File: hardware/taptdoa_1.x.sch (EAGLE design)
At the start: 78 parts, among them J5 105017-0001, U1 SN74HCT245PWR, U2 AP2112K-3.3TRG1, U3 STM32F103RBT6, Y1 8MHz

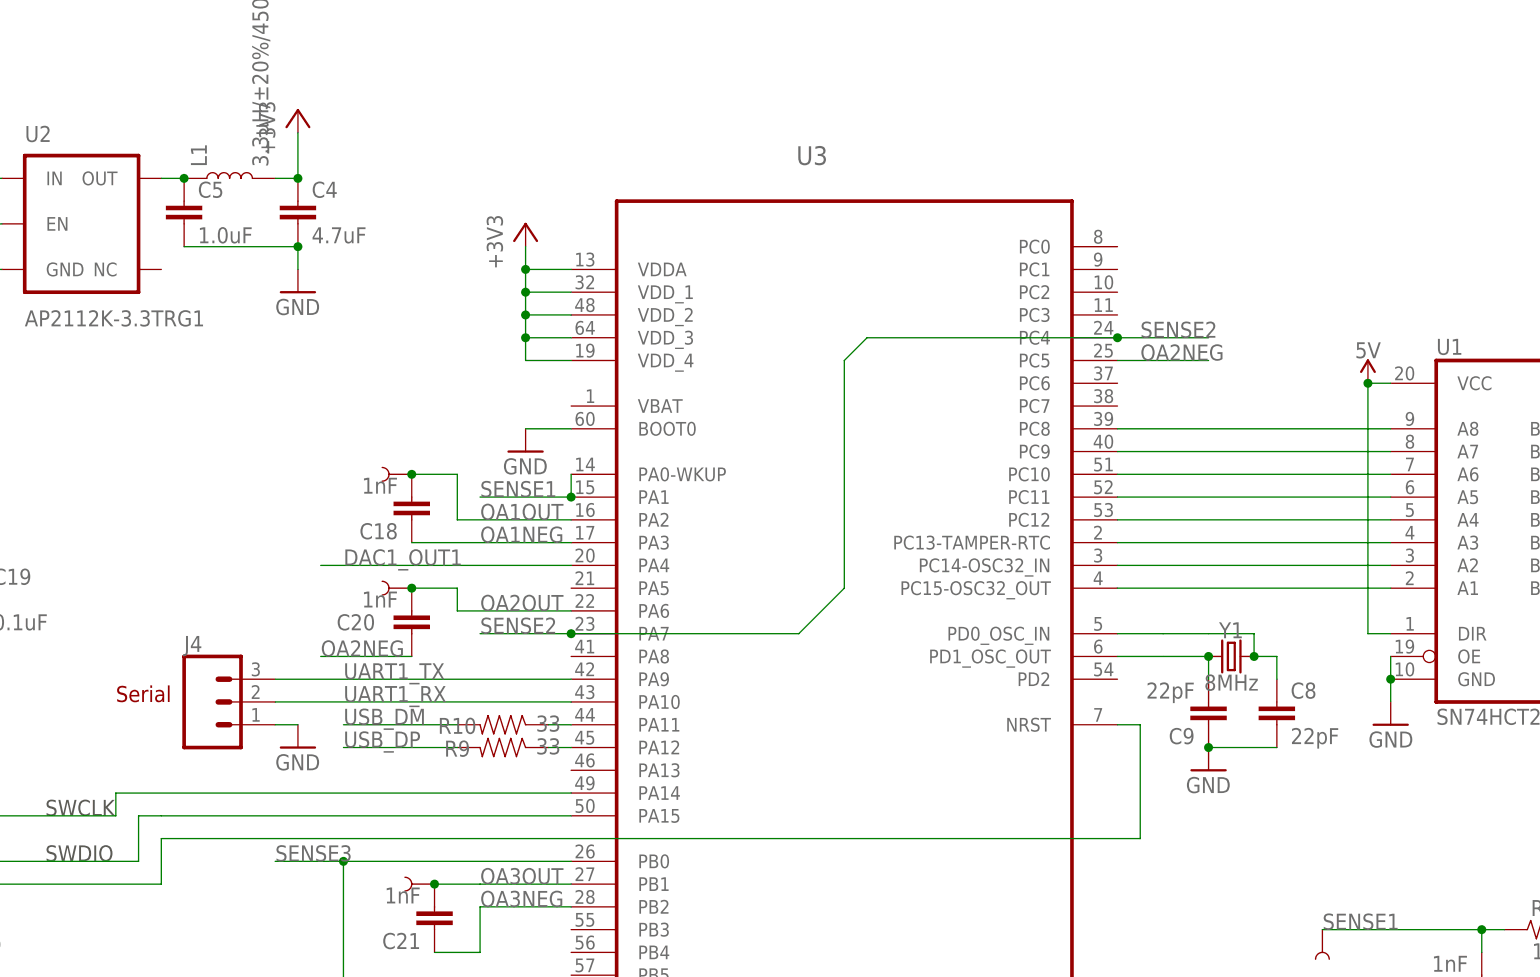
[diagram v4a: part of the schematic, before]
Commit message: new board rev with leds, fix swd pins
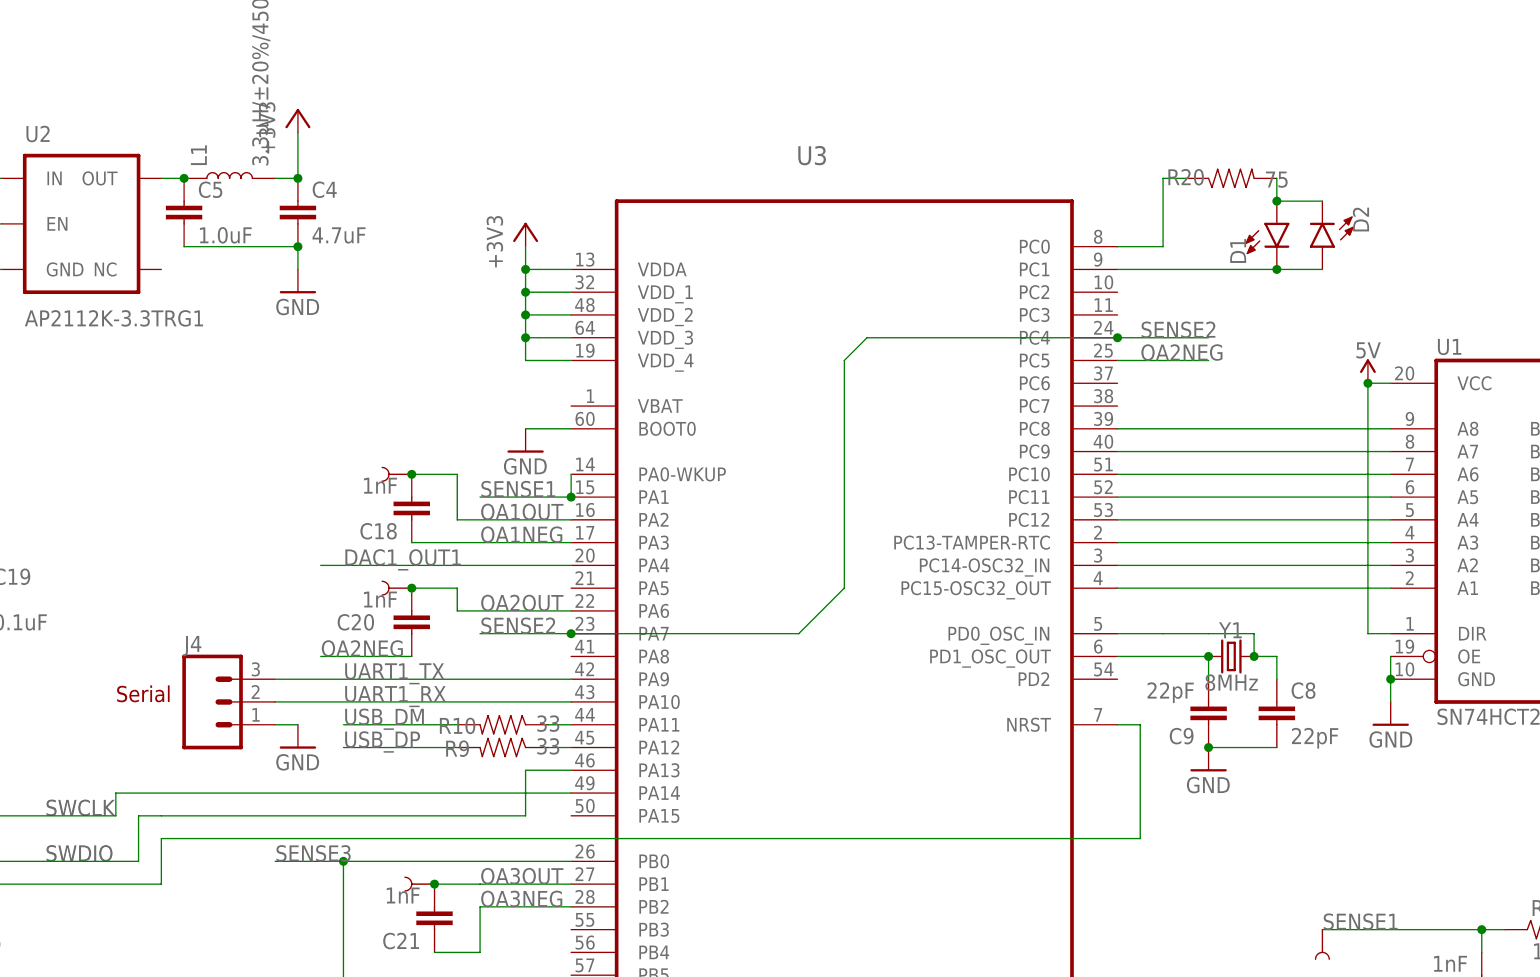
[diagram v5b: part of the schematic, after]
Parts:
- added D1, D2: (no value), SparkFun-LED:LED0603
- added R20: 75, SparkFun-Resistors:100OHM-0603-1/4W-5%
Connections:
- net N$2 renamed PC8
- net N$22 renamed PC12
- net N$24 renamed PC13
- net N$25 renamed PC14
- net N$26 renamed PC15
- net N$4 renamed PC9
- net N$6 renamed PC10
- net N$8 renamed PC11
- new net N$1: R20.1, U3.PC0
- new net N$2: D1.A, D2.C, R20.2
- new net N$3: D1.C, D2.A, U3.PC1
- net PA13: now also U3.PA13; no longer U3.PA15
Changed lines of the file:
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@@
 <part name="TP12" library="SparkFun-Connectors" library_urn="urn:adsk.eagle:library:513" deviceset="TEST-POINT" device="3X4" package3d_urn="urn:adsk.eagle:package:38287/1"/>
 <part name="TP13" library="SparkFun-Connectors" library_urn="urn:adsk.eagle:library:513" deviceset="TEST-POINT" device="3X4" package3d_urn="urn:adsk.eagle:package:38287/1"/>
+<part name="D1" library="SparkFun-LED" library_urn="urn:adsk.eagle:library:529" deviceset="LED" device="0603" package3d_urn="urn:adsk.eagle:package:39354/1"/>
+<part name="D2" library="SparkFun-LED" library_urn="urn:adsk.eagle:library:529" deviceset="LED" device="0603" package3d_urn="urn:adsk.eagle:package:39354/1"/>
+<part name="R20" library="SparkFun-Resistors" library_urn="urn:adsk.eagle:library:532" deviceset="100OHM" device="-0603-1/4W-5%" package3d_urn="urn:adsk.eagle:package:39650/1" value="75"/>
 </parts>
 <sheets>
@@
 <instance part="TP12" gate="G$1" x="154.94" y="25.4" smashed="yes" rot="MR90"/>
 <instance part="TP13" gate="G$1" x="154.94" y="10.16" smashed="yes" rot="MR90"/>
+<instance part="D1" gate="G$1" x="116.84" y="137.16"/>
+<instance part="D2" gate="G$1" x="121.92" y="134.62" rot="R180"/>
+<instance part="R20" gate="G$1" x="111.76" y="142.24" smashed="yes" rot="MR180">
+<attribute name="NAME" x="106.68" y="143.256" size="1.778" layer="95" font="vector" rot="MR180" align="bottom-center"/>
+<attribute name="VALUE" x="116.84" y="141.224" size="1.778" layer="96" font="vector" rot="MR180" align="top-center"/>
+</instance>
 </instances>
 <busses>
@@
 <pinref part="J3" gate="G$1" pin="2"/>
 <wire x1="-30.48" y1="66.04" x2="-27.94" y2="66.04" width="0.1524" layer="91"/>
-<pinref part="U3" gate="A" pin="PA15"/>
-<wire x1="38.1" y1="71.12" x2="-7.62" y2="71.12" width="0.1524" layer="91"/>
 <wire x1="-7.62" y1="71.12" x2="-10.16" y2="71.12" width="0.1524" layer="91"/>
 <wire x1="-10.16" y1="71.12" x2="-10.16" y2="66.04" width="0.1524" layer="91"/>
 <wire x1="-10.16" y1="66.04" x2="-27.94" y2="66.04" width="0.1524" layer="91"/>
+<wire x1="-7.62" y1="71.12" x2="33.02" y2="71.12" width="0.1524" layer="91"/>
+<wire x1="33.02" y1="71.12" x2="33.02" y2="76.2" width="0.1524" layer="91"/>
+<pinref part="U3" gate="A" pin="PA13"/>
+<wire x1="33.02" y1="76.2" x2="38.1" y2="76.2" width="0.1524" layer="91"/>
 </segment>
 </net>
@@
 </segment>
 </net>
-<net name="N$2" class="0">
+<net name="PC8" class="0">
 <segment>
 <pinref part="U1" gate="A" pin="A8"/>
@@
 </segment>
 </net>
-<net name="N$4" class="0">
+<net name="PC9" class="0">
 <segment>
 <pinref part="U1" gate="A" pin="A7"/>
@@
 </segment>
 </net>
-<net name="N$6" class="0">
+<net name="PC10" class="0">
 <segment>
 <pinref part="U3" gate="A" pin="PC10"/>
@@
 </segment>
 </net>
-<net name="N$8" class="0">
+<net name="PC11" class="0">
 <segment>
 <pinref part="U1" gate="A" pin="A5"/>
@@
 </segment>
 </net>
-<net name="N$22" class="0">
+<net name="PC12" class="0">
 <segment>
 <pinref part="U3" gate="A" pin="PC12"/>
@@
 </segment>
 </net>
-<net name="N$24" class="0">
+<net name="PC13" class="0">
 <segment>
 <pinref part="U1" gate="A" pin="A3"/>
@@
 </segment>
 </net>
-<net name="N$25" class="0">
+<net name="PC14" class="0">
 <segment>
 <pinref part="U3" gate="A" pin="PC14-OSC32_IN"/>
@@
 </segment>
 </net>
-<net name="N$26" class="0">
+<net name="PC15" class="0">
 <segment>
 <pinref part="U1" gate="A" pin="A1"/>
@@
 </segment>
 </net>
+<net name="N$1" class="0">
+<segment>
+<pinref part="U3" gate="A" pin="PC0"/>
+<wire x1="99.06" y1="134.62" x2="104.14" y2="134.62" width="0.1524" layer="91"/>
+<wire x1="104.14" y1="134.62" x2="104.14" y2="142.24" width="0.1524" layer="91"/>
+<pinref part="R20" gate="G$1" pin="1"/>
+<wire x1="104.14" y1="142.24" x2="106.68" y2="142.24" width="0.1524" layer="91"/>
+</segment>
+</net>
+<net name="N$2" class="0">
+<segment>
+<pinref part="R20" gate="G$1" pin="2"/>
+<pinref part="D1" gate="G$1" pin="A"/>
+<wire x1="116.84" y1="142.24" x2="116.84" y2="139.7" width="0.1524" layer="91"/>
+<pinref part="D2" gate="G$1" pin="C"/>
+<wire x1="116.84" y1="139.7" x2="121.92" y2="139.7" width="0.1524" layer="91"/>
+<junction x="116.84" y="139.7"/>
+</segment>
+</net>
+<net name="N$3" class="0">
+<segment>
+<pinref part="D2" gate="G$1" pin="A"/>
+<pinref part="D1" gate="G$1" pin="C"/>
+<wire x1="121.92" y1="132.08" x2="116.84" y2="132.08" width="0.1524" layer="91"/>
+<pinref part="U3" gate="A" pin="PC1"/>
+<wire x1="116.84" y1="132.08" x2="99.06" y2="132.08" width="0.1524" layer="91"/>
+<junction x="116.84" y="132.08"/>
+</segment>
+</net>

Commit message: more LEDs
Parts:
- added D3, D4, D5, D6: (no value), SparkFun-LED:LED0603
- added R21, R22, R23, R24: 10k, SparkFun-Resistors:RESISTOR0603
- added R25, R26: 33, SparkFun-Resistors:100OHM-0603-1/4W-5%
- R20: value 75 -> 33
- U3: value STM32F103RBT6 -> STM32F303RET6
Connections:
- removed net N$3: D1.C, D2.A, U3.PC1
- new net N$22: D3.C, D4.A, D5.C, D6.A, R25.2
- new net N$4: R25.1, U3.PC2
- new net N$5: R26.1, U3.PC1
- new net N$6: D1.C, D2.A, D3.A, D4.C, R26.2
- net +3V3: now also R21.2, R22.2, R23.2, R24.2
- net N$19: now also R22.1
- net N$2: now also D5.A, D6.C
- net N$20: now also R24.1
- net N$21: now also R21.1
- net N$23: now also R23.1
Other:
- moved on the sheet: D1, D2, R20

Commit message: fix minor drc
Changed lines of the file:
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@@
 <wire x1="121.92" y1="137.16" x2="129.54" y2="137.16" width="0.1524" layer="91"/>
 <junction x="129.54" y="137.16"/>
+<junction x="134.62" y="137.16"/>
 </segment>
 </net>
@@
 </sheet>
 </sheets>
+<errors>
+</errors>
 </schematic>
 </drawing>
